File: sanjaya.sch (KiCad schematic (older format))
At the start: 0 parts

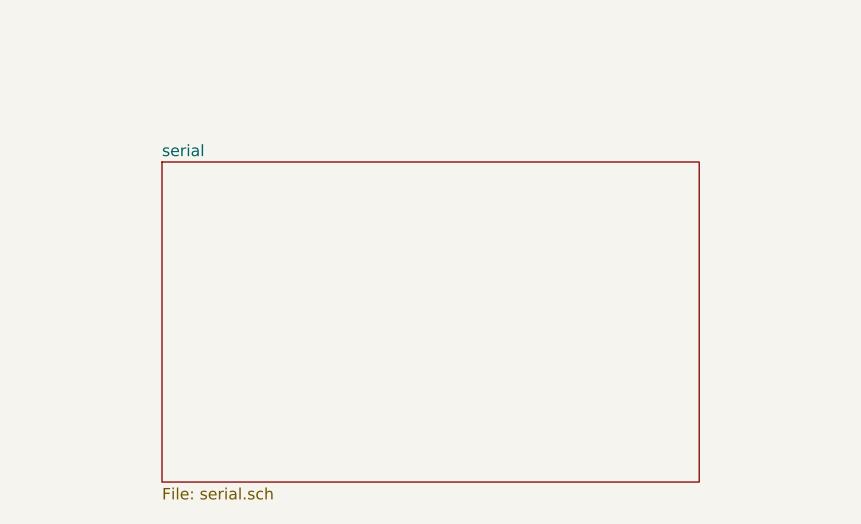
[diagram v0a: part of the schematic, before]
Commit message: Changes: 1. Serial (RS232, 485) circuit added.
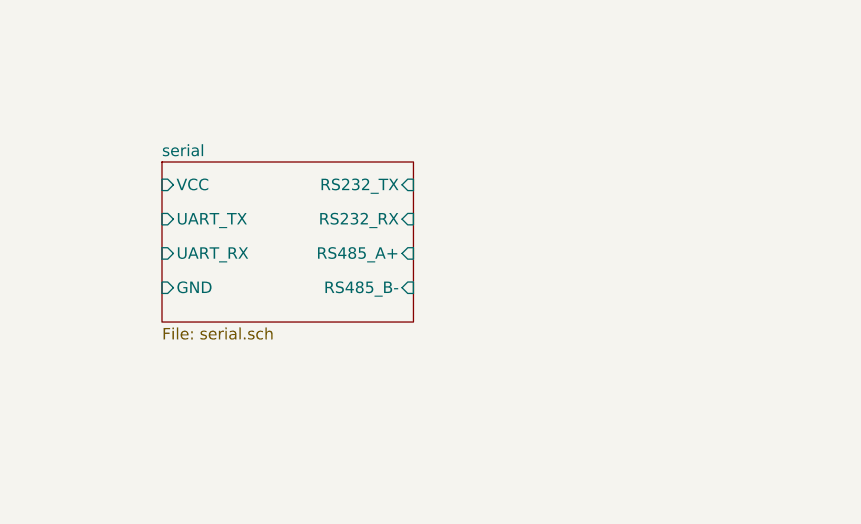
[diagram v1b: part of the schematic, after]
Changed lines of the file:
@@
 EESchema Schematic File Version 4
+LIBS:sanjaya-cache
 EELAYER 26 0
 EELAYER END
@@
 Sheet 1 7
 Title "Sanjaya Gateway"
-Date "2018-09-25"
-Rev "0.1"
+Date "2018-09-29"
+Rev "0.2"
 Comp "Bodhileaf Technologies"
 Comment1 ""
@@
 $EndSheet
 $Sheet
-S 4050 4250 2350 1400
+S 4050 4250 1100 700
 U 5BAA565C
 F0 "serial" 50
 F1 "serial.sch" 50
+F2 "GND" I L 4050 4800 50
+F3 "VCC" I L 4050 4350 50
+F4 "UART_TX" I L 4050 4500 50
+F5 "UART_RX" I L 4050 4650 50
+F6 "RS485_A+" I R 5150 4650 50
+F7 "RS485_B-" I R 5150 4800 50
+F8 "RS232_TX" I R 5150 4350 50
+F9 "RS232_RX" I R 5150 4500 50
 $EndSheet
 $EndSCHEMATC

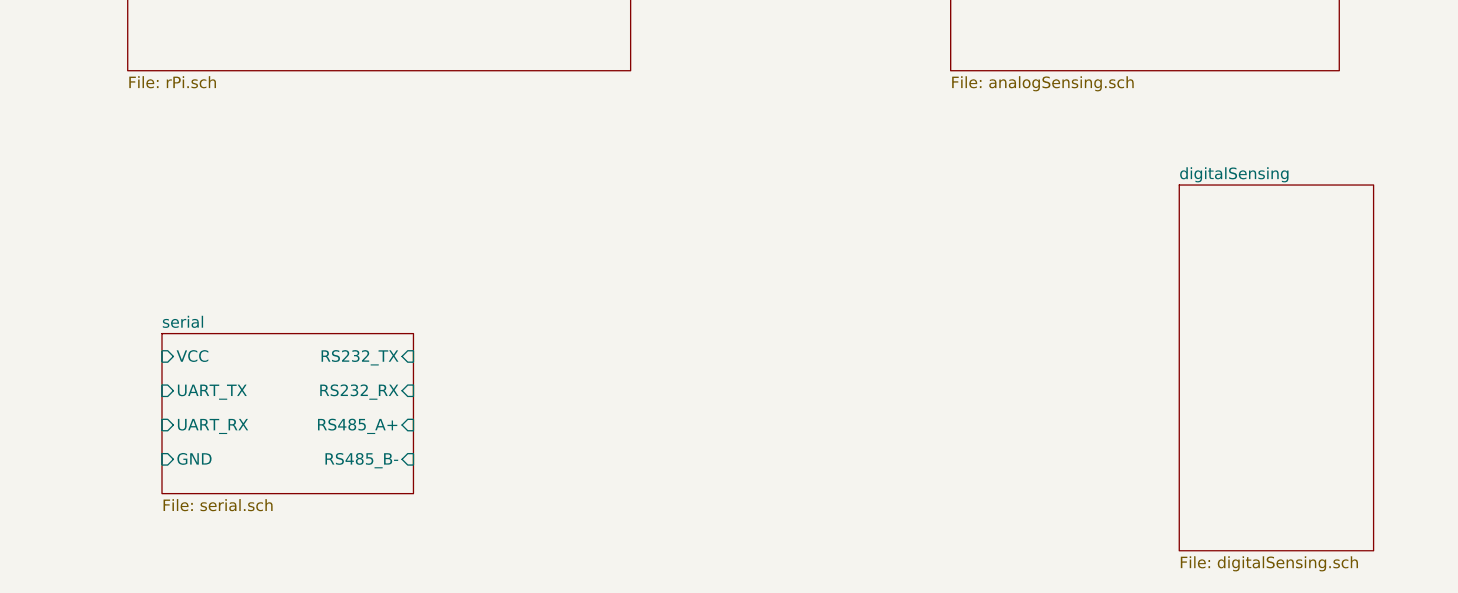
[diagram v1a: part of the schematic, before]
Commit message: Changes: 1. Digital sensing circuit added.
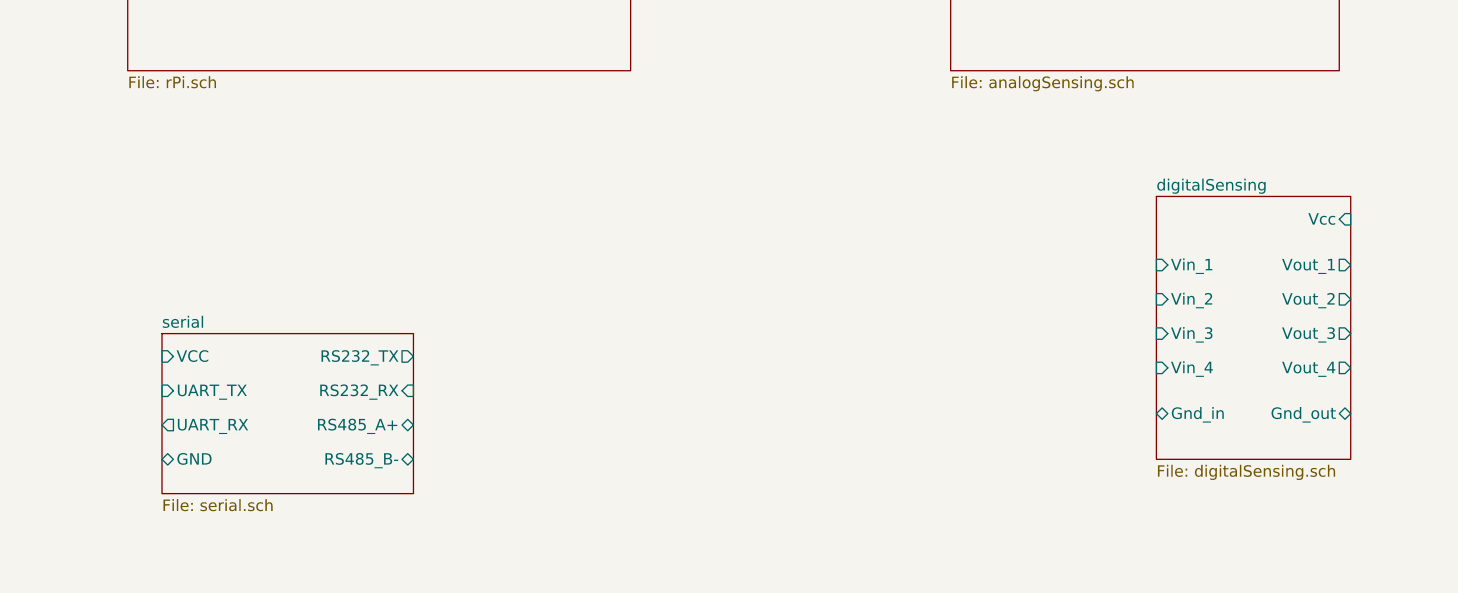
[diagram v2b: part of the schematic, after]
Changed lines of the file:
@@
 Title "Sanjaya Gateway"
 Date "2018-09-29"
-Rev "0.2"
+Rev "0.3"
 Comp "Bodhileaf Technologies"
 Comment1 ""
@@
 $EndSheet
 $Sheet
-S 8500 3600 850  1600
+S 8400 3650 850  1150
 U 5BAA5631
 F0 "digitalSensing" 50
 F1 "digitalSensing.sch" 50
+F2 "Vin_1" I L 8400 3950 50
+F3 "Gnd_in" B L 8400 4600 50
+F4 "Vin_2" I L 8400 4100 50
+F5 "Vin_3" I L 8400 4250 50
+F6 "Vin_4" I L 8400 4400 50
+F7 "Gnd_out" B R 9250 4600 50
+F8 "Vcc" I R 9250 3750 50
+F9 "Vout_1" O R 9250 3950 50
+F10 "Vout_2" O R 9250 4100 50
+F11 "Vout_3" O R 9250 4250 50
+F12 "Vout_4" O R 9250 4400 50
 $EndSheet
 $Sheet
@@
 F0 "serial" 50
 F1 "serial.sch" 50
-F2 "GND" I L 4050 4800 50
-F3 "VCC" I L 4050 4350 50
-F4 "UART_TX" I L 4050 4500 50
-F5 "UART_RX" I L 4050 4650 50
-F6 "RS485_A+" I R 5150 4650 50
-F7 "RS485_B-" I R 5150 4800 50
-F8 "RS232_TX" I R 5150 4350 50
+F2 "VCC" I L 4050 4350 50
+F3 "UART_TX" I L 4050 4500 50
+F4 "GND" B L 4050 4800 50
+F5 "UART_RX" O L 4050 4650 50
+F6 "RS485_A+" B R 5150 4650 50
+F7 "RS485_B-" B R 5150 4800 50
+F8 "RS232_TX" O R 5150 4350 50
 F9 "RS232_RX" I R 5150 4500 50
 $EndSheet

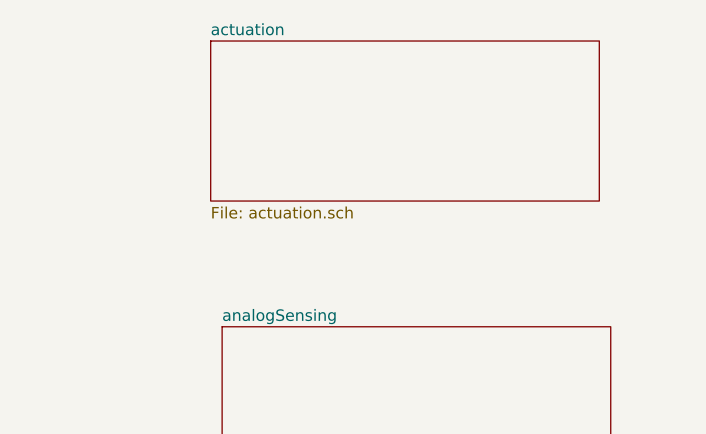
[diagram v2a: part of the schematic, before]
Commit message: Changes: 1. Relay and partial analog sensing circuitry added.
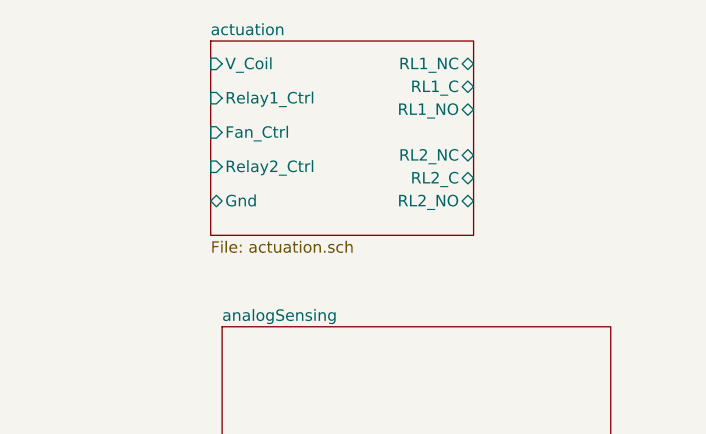
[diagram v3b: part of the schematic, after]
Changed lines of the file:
@@
 $EndSheet
 $Sheet
-S 7450 1100 1700 700
+S 7450 1100 1150 850
 U 5BAA55AD
 F0 "actuation" 50
 F1 "actuation.sch" 50
+F2 "V_Coil" I L 7450 1200 50
+F3 "Gnd" B L 7450 1800 50
+F4 "Relay1_Ctrl" I L 7450 1350 50
+F5 "Fan_Ctrl" I L 7450 1500 50
+F6 "Relay2_Ctrl" I L 7450 1650 50
+F7 "RL1_NO" B R 8600 1400 50
+F8 "RL1_NC" B R 8600 1200 50
+F9 "RL1_C" B R 8600 1300 50
+F10 "RL2_C" B R 8600 1700 50
+F11 "RL2_NC" B R 8600 1600 50
+F12 "RL2_NO" B R 8600 1800 50
 $EndSheet
 $Sheet

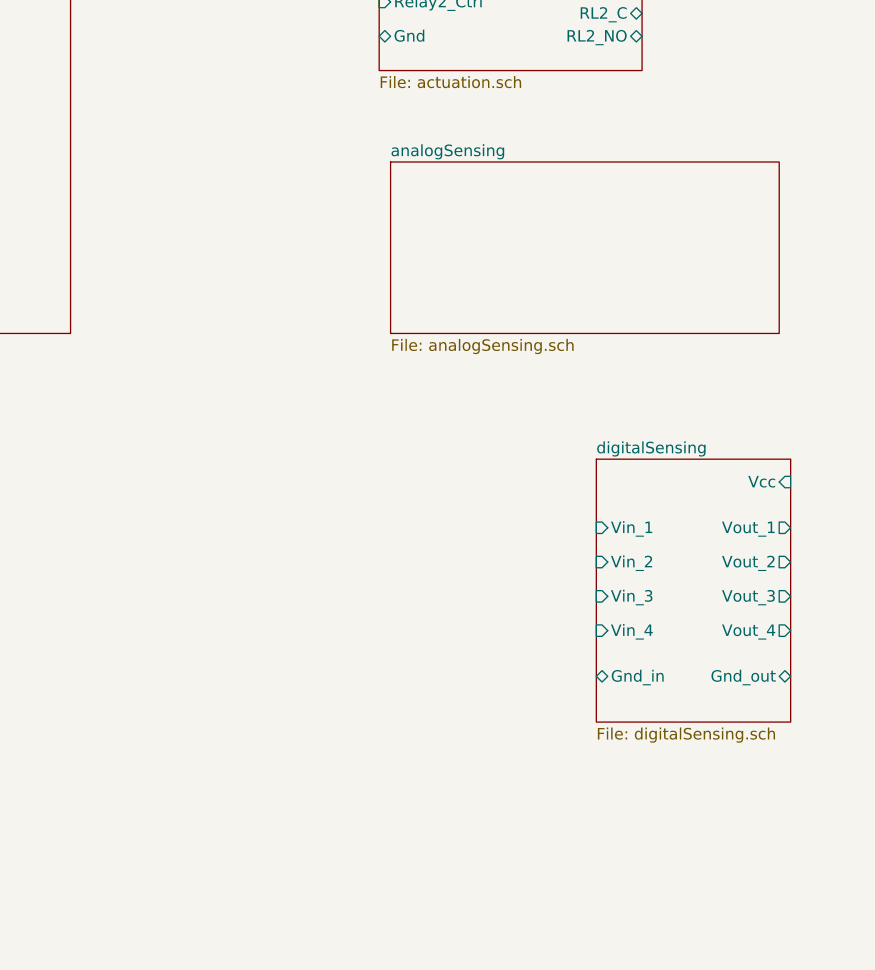
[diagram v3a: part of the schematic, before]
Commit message: Changes: 1. Added Analog circuitry
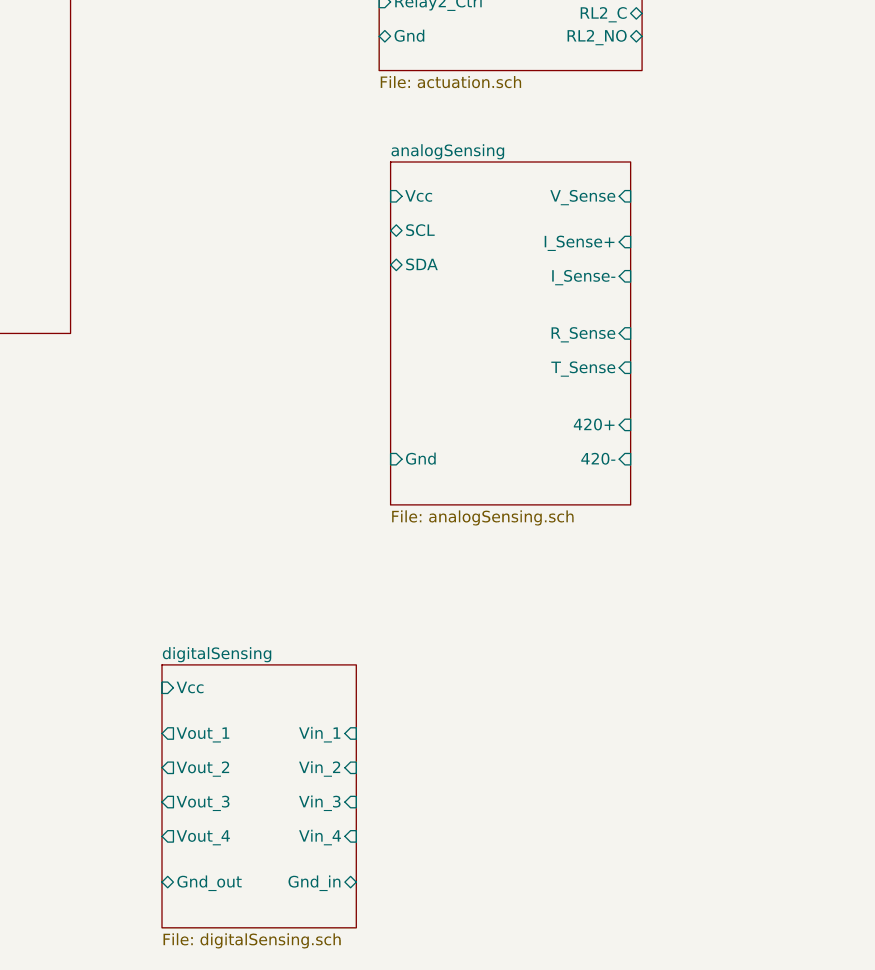
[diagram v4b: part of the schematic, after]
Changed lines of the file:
@@
 Sheet 1 7
 Title "Sanjaya Gateway"
-Date "2018-09-29"
-Rev "0.3"
+Date "2018-10-01"
+Rev "0.4"
 Comp "Bodhileaf Technologies"
 Comment1 ""
@@
 $EndSheet
 $Sheet
-S 7500 2350 1700 750
+S 7500 2350 1050 1500
 U 5BAA5602
 F0 "analogSensing" 50
 F1 "analogSensing.sch" 50
+F2 "Vcc" I L 7500 2500 50
+F3 "Gnd" I L 7500 3650 50
+F4 "SCL" B L 7500 2650 50
+F5 "SDA" B L 7500 2800 50
+F6 "V_Sense" I R 8550 2500 50
+F7 "I_Sense+" I R 8550 2700 50
+F8 "I_Sense-" I R 8550 2850 50
+F9 "R_Sense" I R 8550 3100 50
+F10 "T_Sense" I R 8550 3250 50
+F11 "420+" I R 8550 3500 50
+F12 "420-" I R 8550 3650 50
 $EndSheet
 $Sheet
-S 8400 3650 850  1150
+S 6500 4550 850  1150
 U 5BAA5631
 F0 "digitalSensing" 50
 F1 "digitalSensing.sch" 50
-F2 "Vin_1" I L 8400 3950 50
-F3 "Gnd_in" B L 8400 4600 50
-F4 "Vin_2" I L 8400 4100 50
-F5 "Vin_3" I L 8400 4250 50
-F6 "Vin_4" I L 8400 4400 50
-F7 "Gnd_out" B R 9250 4600 50
-F8 "Vcc" I R 9250 3750 50
-F9 "Vout_1" O R 9250 3950 50
-F10 "Vout_2" O R 9250 4100 50
-F11 "Vout_3" O R 9250 4250 50
-F12 "Vout_4" O R 9250 4400 50
+F2 "Vin_1" I R 7350 4850 50
+F3 "Gnd_in" B R 7350 5500 50
+F4 "Vin_2" I R 7350 5000 50
+F5 "Vin_3" I R 7350 5150 50
+F6 "Vin_4" I R 7350 5300 50
+F7 "Gnd_out" B L 6500 5500 50
+F8 "Vcc" I L 6500 4650 50
+F9 "Vout_1" O L 6500 4850 50
+F10 "Vout_2" O L 6500 5000 50
+F11 "Vout_3" O L 6500 5150 50
+F12 "Vout_4" O L 6500 5300 50
 $EndSheet
 $Sheet

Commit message: Changes: 1. RPi hierarchial sheet populated with appropriate circuit 2. Wiring hierarchial sheets together completed except for the temperature sensor
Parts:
- added J?: PWR_SUPPLY, symbol Connector:Screw_Terminal_01x02
- added J?: Digital_Input_Signals, symbol Connector:Screw_Terminal_01x04
- added J?: Digital_input_Gnd, symbol Connector:Screw_Terminal_01x02
- added J? (x2): Screw_Terminal_01x02, symbol Connector:Screw_Terminal_01x02
- added J? (x2): Screw_Terminal_01x03, symbol Connector:Screw_Terminal_01x03
- added R?: 20m, symbol Device:R_Small
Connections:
- net labels added: 3V3, AGND, DGND, D_INPUT_A, D_INPUT_B, D_INPUT_C, D_INPUT_D, I_Sense+, I_Sense-
- wire segments 0 -> 69

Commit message: Changes: 1. Added temperature sensor 2. Wired it to the rest of the circuit making this the first full-fledged schematic
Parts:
- added U?: MCP9700T-ETT, Package_TO_SOT_SMD:SOT-23, symbol Sensor_Temperature:MCP9700T-ETT
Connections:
- wire segments 69 -> 76
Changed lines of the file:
@@
 Sheet 1 7
 Title "Sanjaya Gateway"
-Date "2018-10-01"
-Rev "0.5"
+Date "2018-10-02"
+Rev "0.6"
 Comp "Bodhileaf Technologies"
 Comment1 ""
@@
 $EndSheet
 $Sheet
-S 5550 5000 850  1150
+S 5550 5200 850  1150
 U 5BAA5631
 F0 "digitalSensing" 50
 F1 "digitalSensing.sch" 50
-F2 "Vin_1" I R 6400 5300 50
-F3 "Gnd_in" B R 6400 5800 50
-F4 "Vin_2" I R 6400 5400 50
-F5 "Vin_3" I R 6400 5500 50
-F6 "Vin_4" I R 6400 5600 50
-F7 "Gnd_out" B L 5550 5800 50
-F8 "Vcc" I L 5550 5100 50
-F9 "Vout_1" O L 5550 5300 50
-F10 "Vout_2" O L 5550 5400 50
-F11 "Vout_3" O L 5550 5500 50
-F12 "Vout_4" O L 5550 5600 50
+F2 "Vin_1" I R 6400 5500 50
+F3 "Gnd_in" B R 6400 6000 50
+F4 "Vin_2" I R 6400 5600 50
+F5 "Vin_3" I R 6400 5700 50
+F6 "Vin_4" I R 6400 5800 50
+F7 "Gnd_out" B L 5550 6000 50
+F8 "Vcc" I L 5550 5300 50
+F9 "Vout_1" O L 5550 5500 50
+F10 "Vout_2" O L 5550 5600 50
+F11 "Vout_3" O L 5550 5700 50
+F12 "Vout_4" O L 5550 5800 50
 $EndSheet
 $Sheet
@@
 Text Label 4800 3150 2    50   ~ 0
 D_INPUT_D
+Text Label 5300 5500 2    50   ~ 0
+D_INPUT_A
+Text Label 5300 5600 2    50   ~ 0
+D_INPUT_B
+Text Label 5300 5700 2    50   ~ 0
+D_INPUT_C
+Text Label 5300 5800 2    50   ~ 0
+D_INPUT_D
+Wire Wire Line
+	4800 2850 5000 2850
+Wire Wire Line
+	5000 2950 4800 2950
+Wire Wire Line
+	4800 3050 5000 3050
+Wire Wire Line
+	5000 3150 4800 3150
+Wire Wire Line
+	5300 5500 5550 5500
+Wire Wire Line
+	5300 5600 5550 5600
+Wire Wire Line
+	5300 5700 5550 5700
+Wire Wire Line
+	5300 5800 5550 5800
+Text Label 5300 6000 2    50   ~ 0
+DGND
+Wire Wire Line
+	5300 6000 5550 6000
 Text Label 5300 5300 2    50   ~ 0
-D_INPUT_A
-Text Label 5300 5400 2    50   ~ 0
-D_INPUT_B
-Text Label 5300 5500 2    50   ~ 0
-D_INPUT_C
-Text Label 5300 5600 2    50   ~ 0
-D_INPUT_D
-Wire Wire Line
-	4800 2850 5000 2850
-Wire Wire Line
-	5000 2950 4800 2950
-Wire Wire Line
-	4800 3050 5000 3050
-Wire Wire Line
-	5000 3150 4800 3150
+3V3
 Wire Wire Line
 	5300 5300 5550 5300
-Wire Wire Line
-	5300 5400 5550 5400
-Wire Wire Line
-	5300 5500 5550 5500
-Wire Wire Line
-	5300 5600 5550 5600
-Text Label 5300 5800 2    50   ~ 0
-DGND
-Wire Wire Line
-	5300 5800 5550 5800
-Text Label 5300 5100 2    50   ~ 0
-3V3
-Wire Wire Line
-	5300 5100 5550 5100
 $Comp
 L Connector:Screw_Terminal_01x04 J?
 U 1 1 5BB4878D
-P 6800 5400
-F 0 "J?" H 6880 5392 50  0000 L CNN
-F 1 "Digital_Input_Signals" H 6880 5301 50  0000 L CNN
-F 2 "" H 6800 5400 50  0001 C CNN
-F 3 "~" H 6800 5400 50  0001 C CNN
-	1    6800 5400
-	1    0    0    -1
-$EndComp
-Wire Wire Line
-	6400 5300 6600 5300
-Wire Wire Line
-	6400 5400 6600 5400
+P 6800 5600
+F 0 "J?" H 6880 5592 50  0000 L CNN
+F 1 "Digital_Input_Signals" H 6880 5501 50  0000 L CNN
+F 2 "" H 6800 5600 50  0001 C CNN
+F 3 "~" H 6800 5600 50  0001 C CNN
+	1    6800 5600
+	1    0    0    -1
+$EndComp
 Wire Wire Line
 	6400 5500 6600 5500
 Wire Wire Line
-	6600 5600 6400 5600
+	6400 5600 6600 5600
+Wire Wire Line
+	6400 5700 6600 5700
+Wire Wire Line
+	6600 5800 6400 5800
 $Comp
 L Connector:Screw_Terminal_01x02 J?
 U 1 1 5BB4CAA3
-P 6800 5800
-F 0 "J?" H 6879 5792 50  0000 L CNN
-F 1 "Digital_input_Gnd" H 6879 5701 50  0000 L CNN
-F 2 "" H 6800 5800 50  0001 C CNN
-F 3 "~" H 6800 5800 50  0001 C CNN
-	1    6800 5800
-	1    0    0    -1
-$EndComp
-Wire Wire Line
-	6400 5800 6500 5800
-Wire Wire Line
-	6600 5900 6500 5900
-Wire Wire Line
-	6500 5900 6500 5800
-Connection ~ 6500 5800
-Wire Wire Line
-	6500 5800 6600 5800
+P 6800 6000
+F 0 "J?" H 6879 5992 50  0000 L CNN
+F 1 "Digital_input_Gnd" H 6879 5901 50  0000 L CNN
+F 2 "" H 6800 6000 50  0001 C CNN
+F 3 "~" H 6800 6000 50  0001 C CNN
+	1    6800 6000
+	1    0    0    -1
+$EndComp
+Wire Wire Line
+	6400 6000 6500 6000
+Wire Wire Line
+	6600 6100 6500 6100
+Wire Wire Line
+	6500 6100 6500 6000
+Connection ~ 6500 6000
+Wire Wire Line
+	6500 6000 6600 6000
 $Comp
 L Connector:Screw_Terminal_01x02 J?
@@
 Wire Wire Line
 	8650 3250 8900 3250
+$Comp
+L Sensor_Temperature:MCP9700T-ETT U?
+U 1 1 5BB39F58
+P 6000 4550
+F 0 "U?" H 5670 4596 50  0000 R CNN
+F 1 "MCP9700T-ETT" H 5670 4505 50  0000 R CNN
+F 2 "Package_TO_SOT_SMD:SOT-23" H 6000 4150 50  0001 C CNN
+F 3 "http://ww1.microchip.com/downloads/en/DeviceDoc/21942e.pdf" H 5850 4800 50  0001 C CNN
+	1    6000 4550
+	1    0    0    -1
+$EndComp
+Text Label 5950 4950 2    50   ~ 0
+AGND
+Wire Wire Line
+	6000 4850 6000 4950
+Wire Wire Line
+	6000 4950 5950 4950
+Text Label 5900 4200 2    50   ~ 0
+3V3
+Wire Wire Line
+	5900 4200 6000 4200
+Wire Wire Line
+	6000 4200 6000 4250
+Wire Wire Line
+	6400 4550 6750 4550
+Wire Wire Line
+	6750 4550 6750 4800
+Wire Wire Line
+	6750 4800 7550 4800
 $EndSCHEMATC
